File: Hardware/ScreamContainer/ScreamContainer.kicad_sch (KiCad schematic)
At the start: 14 parts, among them U1 LOGIC-74HC595N_DIP16_, U2 LOGIC-74HC595N_DIP16_

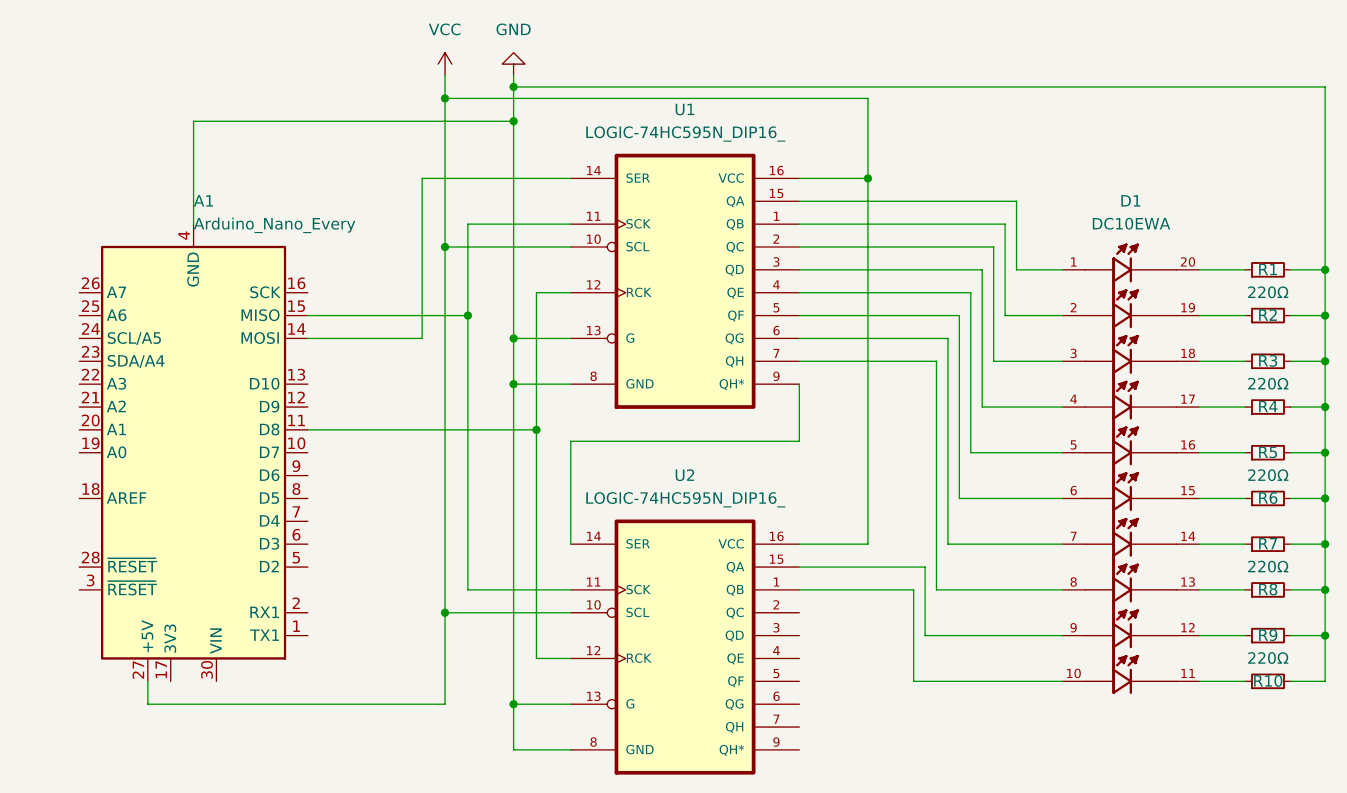
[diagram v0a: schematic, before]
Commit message: Removing some files and adding new symbols
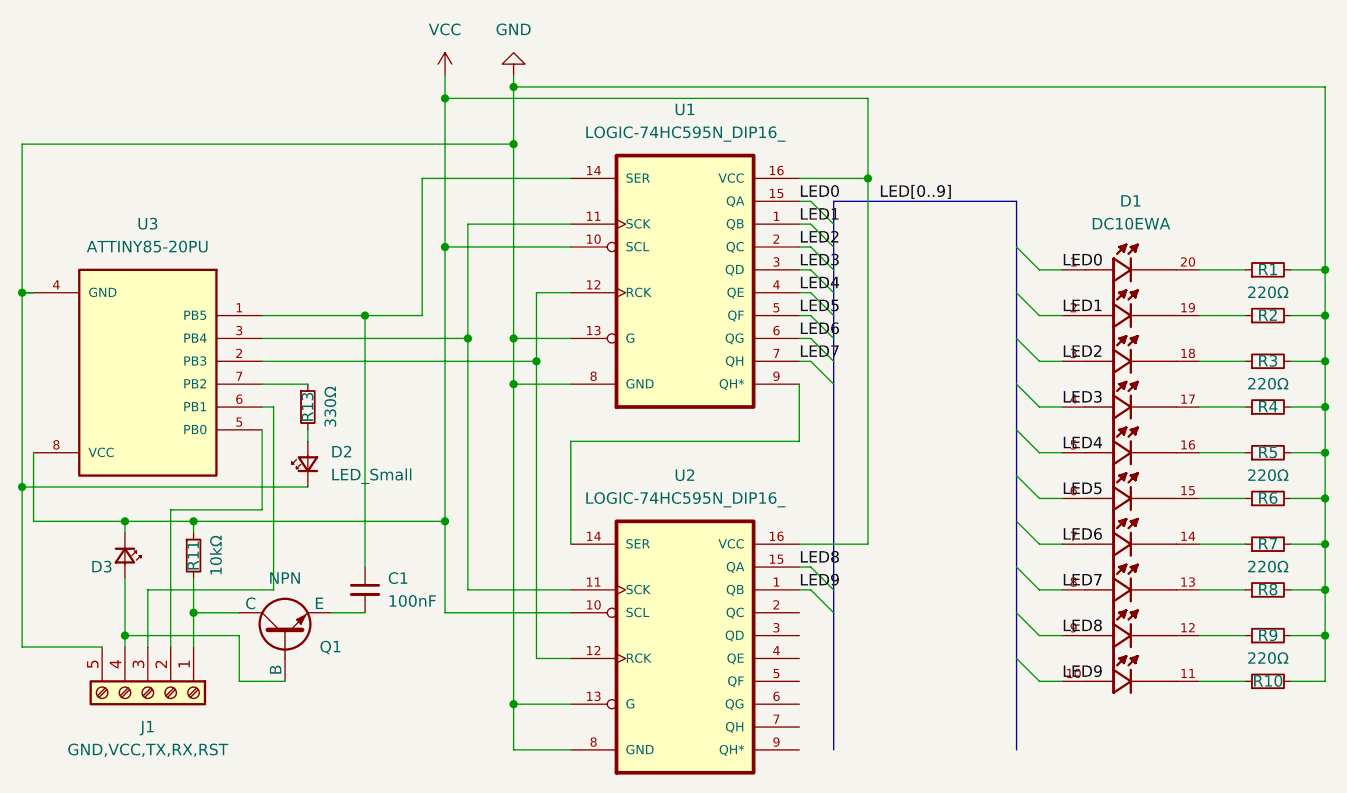
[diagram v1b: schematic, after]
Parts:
- removed A1: Arduino_Nano_Every, Module:Arduino_Nano, symbol MCU_Module:Arduino_Nano_Every
- added C1: 100nF, symbol Device:C_Small
- added D2, D3: LED_Small, symbol Device:LED_Small
- added J1: GND,VCC,TX,RX,RST, symbol Connector:Screw_Terminal_01x05
- added Q1: NPN, symbol Simulation_SPICE:NPN
- added R11: 10kΩ, Resistor_THT:R_Axial_DIN0204_L3.6mm_D1.6mm_P7.62mm_Horizontal, symbol Device:R_Small
- added R13: 330Ω, Resistor_THT:R_Axial_DIN0204_L3.6mm_D1.6mm_P7.62mm_Horizontal, symbol Device:R_Small
- added U3: ATTINY85-20PU, ATTINY85-20PU:DIP762W46P254L927H533Q8B, symbol ATTINY85:ATTINY85-20PU
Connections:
- net GND: now also D2.1 (K), J1.5 (Pin_5), U3.4 (GND)
- net VCC: now also D3.1 (K), R11.1, U3.8 (VCC)
- net LED9: now reaches D1.10, U2.1 (QB)
- net at U1.11 (SCK), U2.11 (SCK): now also U3.3 (PB4)
- net at U1.12 (RCK), U2.12 (RCK): now also U3.2 (PB3)
- net LED8: now reaches D1.9, U2.15 (QA)
- net LED1: now reaches D1.2, U1.1 (QB)
- net at U1.14 (SER): now also C1.1, U3.1 (PB5)
- net LED0: now reaches D1.1, U1.15 (QA)
- net LED2: now reaches D1.3, U1.2 (QC)
- net LED3: now reaches D1.4, U1.3 (QD)
- net LED4: now reaches D1.5, U1.4 (QE)
- net LED5: now reaches D1.6, U1.5 (QF)
- net LED6: now reaches D1.7, U1.6 (QG)
- net LED7: now reaches D1.8, U1.7 (QH)
- new net: D3.2 (A), J1.4 (Pin_4), Q1.2 (B)
- new net: D2.2 (A), R13.2
- new net: J1.2 (Pin_2), U3.5 (PB0)
- new net: J1.3 (Pin_3), U3.6 (PB1)
- new net: R13.1, U3.7 (PB2)
- new net: J1.1 (Pin_1), Q1.1 (C), R11.2
- new net: C1.2, Q1.3 (E)
